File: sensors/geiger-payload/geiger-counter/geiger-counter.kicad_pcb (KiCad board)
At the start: 2 copper layers, 121.3 x 44.7 mm, 38 parts, among them J1 3531, J2 3531, J4 Conn_02x03_Odd_Even, J5 Conn_01x06, J6 Conn_01x03, Q1 MMBTA44, Q2 MMBT3904, Q3 MMBT3904, SW1 SW_Push, SW2 SW_SPDT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

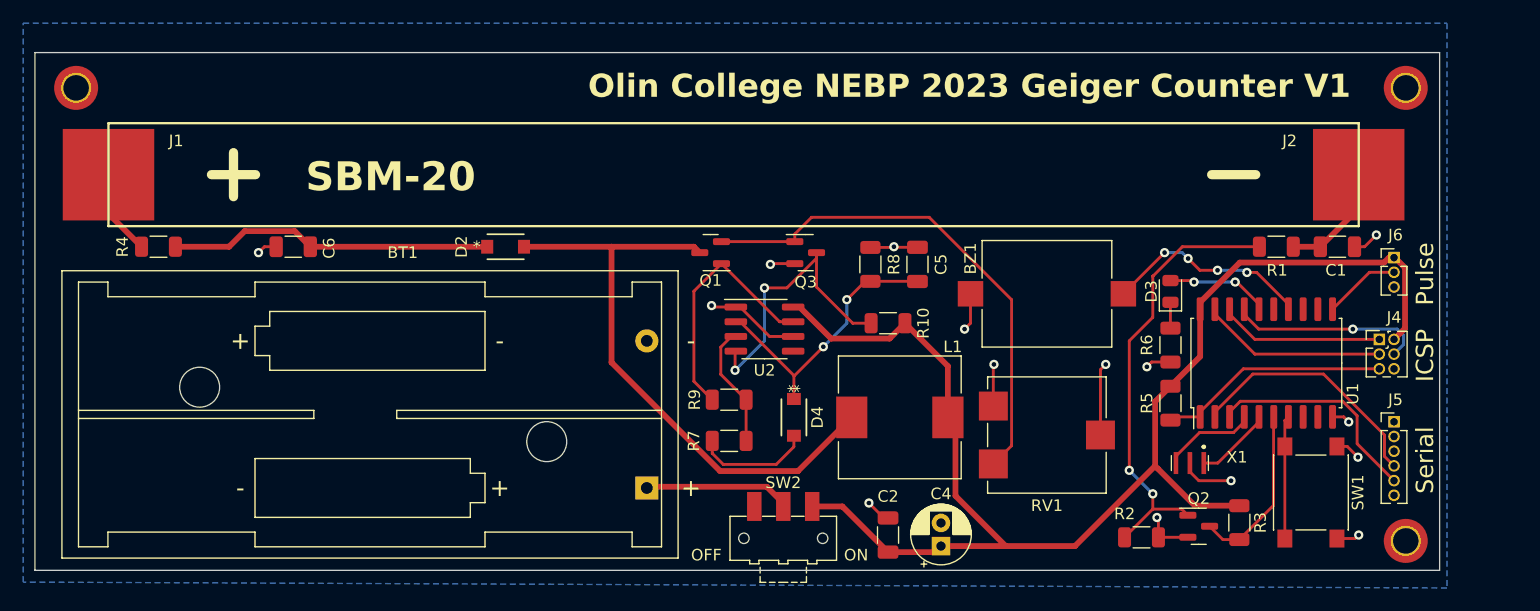
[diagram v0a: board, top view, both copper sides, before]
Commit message: Add pcb corrections
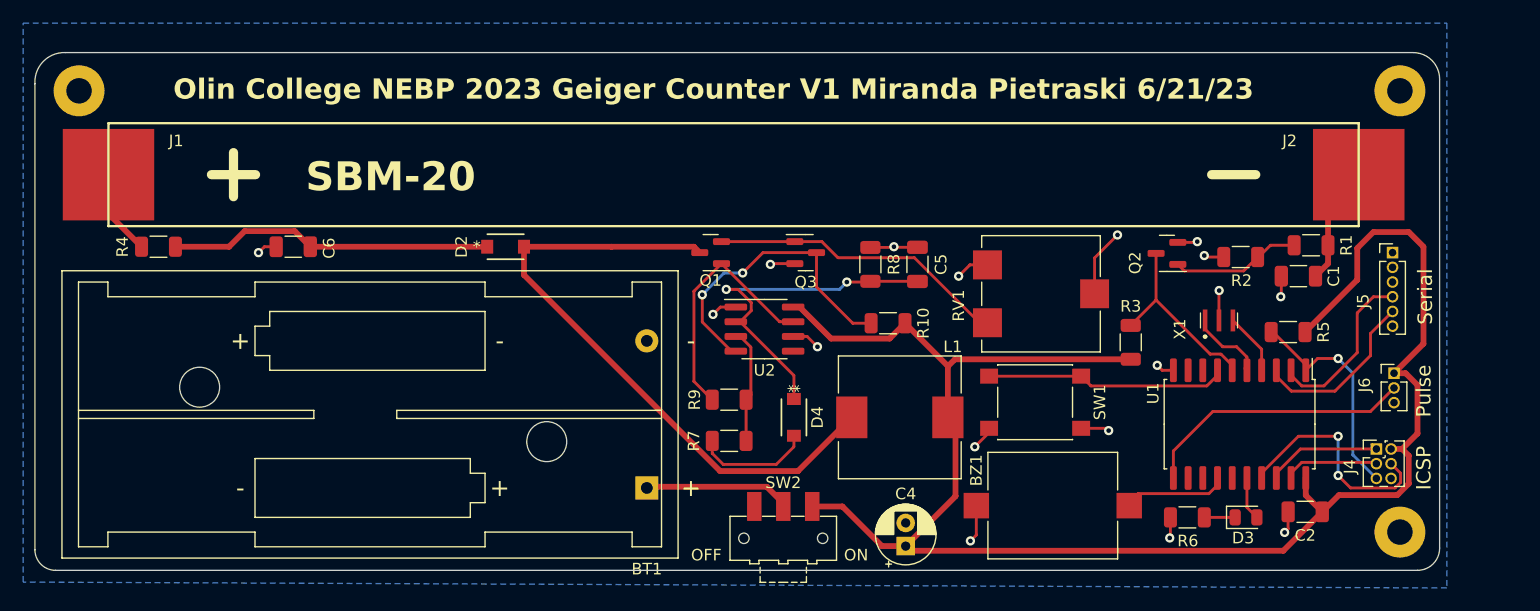
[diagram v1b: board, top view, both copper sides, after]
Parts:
- H1, H2, H3: value MountingHole -> MountingHole_Pad; footprint MountingHole:MountingHole_2.2mm_M2_DIN965_Pad_TopOnly -> MountingHole:MountingHole_2.2mm_M2_Pad
- moved C2 36.1 mm to (198.6, 64.0), turned to 180 degrees
- moved R2 25.7 mm to (193.0, 42.0), turned to 0 degrees
- moved SW1 25.1 mm to (175.3, 54.6), turned to 0 degrees
- moved Q2 23.7 mm to (186.6, 41.7), turned to 180 degrees
- moved D3 20.6 mm to (193.5, 64.5), turned to 0 degrees
- moved BZ1 18.3 mm to (176.8, 63.5)
- moved R3 18.2 mm to (183.5, 49.4), turned to 90 degrees
- moved R6 14.9 mm to (188.4, 64.5), turned to 180 degrees
- moved J5 14.6 mm to (206.1, 41.7)
- moved RV1 12.2 mm to (175.8, 45.2)
- moved R5 11.9 mm to (197.1, 48.5), turned to 180 degrees
- moved X1 11.7 mm to (191.1, 47.9), turned to 0 degrees
- moved J6 9.99 mm to (206.2, 52.1)
- moved J4 9.47 mm to (204.7, 58.6)
- moved U1 5.76 mm to (192.9, 56.5), turned to -90 degrees
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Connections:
- H1 pad 1: (no net) -> GND
- H2 pad 1: (no net) -> GND
- H3 pad 1: (no net) -> GND
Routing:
- net VCC: track 119.2 -> 149.8 mm
- net Net-(Q2-B): track 38.8 -> 11.2 mm, vias 2 -> 0
- net Net-(Q1-E): track 44.1 -> 25.9 mm
- net Net-(J6-Pin_2): track 6.63 -> 23.9 mm
- net Net-(U1-PD3): track 10.6 -> 21.4 mm
- net Net-(BZ1--): track 18.0 -> 9.12 mm, vias 4 -> 0
- net GND: track 50.7 -> 42.8 mm, vias 15 -> 17
- net Net-(J4-Pin_3): track 16.1 -> 8.22 mm
- net Net-(U2-TR): track 24.2 -> 30.9 mm
- net Net-(J5-Pin_4): track 21.6 -> 15.3 mm
- net Net-(D3-A): track 8.92 -> 3.76 mm, vias 2 -> 0
- net Net-(J5-Pin_5): track 19.3 -> 15.0 mm
- net Net-(J4-Pin_1): track 14.3 -> 10.5 mm
- net Net-(Q1-C): track 51.9 -> 55.1 mm
- net Net-(U1-PA1/XTAL2): track 8.15 -> 5.33 mm
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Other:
- outline, holes or cut-outs redrawn
- board text added: "Olin College NEBP 2023 Geiger Counter V1 Miranda Pietraski 6/21/23"
- board text removed: "Olin College NEBP 2023 Geiger Counter V1"

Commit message: add board fixes
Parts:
- moved H2 0.97 mm to (206.4, 26.8)
- moved H3 0.90 mm to (92.8, 26.8)
- moved H1 0.38 mm to (206.4, 65.8)
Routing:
- net Net-(Q1-E): track 25.9 -> 27.8 mm
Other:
- board size 121.3 x 44.7 mm -> 121.3 x 46.1 mm
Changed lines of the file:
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@@
   )
   (footprint "MountingHole:MountingHole_2.2mm_M2_Pad" (layer "F.Cu")
-    (at 206.756 65.786)
+    (at 206.375 65.786)
     (descr "Mounting Hole 2.2mm, M2")
     (tags "mounting hole 2.2mm m2")
@@
   )
   (footprint "MountingHole:MountingHole_2.2mm_M2_Pad" (layer "F.Cu")
-    (at 92.71 27.686)
+    (at 92.837 26.797)
     (descr "Mounting Hole 2.2mm, M2")
     (tags "mounting hole 2.2mm m2")
@@
   )
   (footprint "MountingHole:MountingHole_2.2mm_M2_Pad" (layer "F.Cu")
-    (at 206.756 27.686)
+    (at 206.375 26.797)
     (descr "Mounting Hole 2.2mm, M2")
     (tags "mounting hole 2.2mm m2")
@@
   (gr_line (start 106.045 33.02) (end 106.045 36.83)
     (stroke (width 0.8) (type default)) (layer "F.SilkS"))
+  (gr_arc (start 88.9 26.543) (mid 89.858175 24.034993) (end 92.329 22.984649)
+    (stroke (width 0.1) (type default)) (layer "Edge.Cuts"))
   (gr_arc (start 90.678 69.088) (mid 89.420764 68.567236) (end 88.9 67.31)
-    (stroke (width 0.1) (type default)) (layer "Edge.Cuts"))
-  (gr_arc (start 88.901216 27.07334) (mid 89.633813 25.133633) (end 91.567 24.384)
     (stroke (width 0.1) (type default)) (layer "Edge.Cuts"))
   (gr_arc (start 210.185 67.183) (mid 209.627038 68.530038) (end 208.28 69.088)
     (stroke (width 0.1) (type default)) (layer "Edge.Cuts"))
-  (gr_arc (start 207.899 24.384) (mid 209.515446 25.053554) (end 210.185 26.67)
+  (gr_line (start 92.329 22.984649) (end 207.391 22.987)
     (stroke (width 0.1) (type default)) (layer "Edge.Cuts"))
-  (gr_line (start 210.185 67.183) (end 210.185 26.67)
+  (gr_arc (start 207.391 22.987) (mid 209.366656 23.805344) (end 210.185 25.781)
     (stroke (width 0.1) (type default)) (layer "Edge.Cuts"))
-  (gr_line (start 88.901216 27.07334) (end 88.9 67.31)
+  (gr_line (start 210.185 67.183) (end 210.185 25.781)
     (stroke (width 0.1) (type default)) (layer "Edge.Cuts"))
-  (gr_line (start 207.899 24.384) (end 91.567 24.384)
+  (gr_line (start 88.9 26.543) (end 88.9 67.31)
     (stroke (width 0.1) (type default)) (layer "Edge.Cuts"))
   (gr_line (start 90.678 69.088) (end 208.28 69.088)
@@
     (effects (font (size 1.25 1.25) (thickness 0.1875)) (justify left bottom))
   )
-  (gr_text "Olin College NEBP 2023 Geiger Counter V1 Miranda Pietraski 6/21/23" (at 100.838 28.575) (layer "F.SilkS")
+  (gr_text "Olin College NEBP 2023 Geiger Counter V1 Miranda Pietraski 6/21/23" (at 100.965 27.94) (layer "F.SilkS")
     (effects (font (size 1.75 1.75) (thickness 0.35) bold) (justify left bottom))
   )
@@
   (segment (start 148.179 42.606) (end 153.198 47.625) (width 0.25) (layer "F.Cu") (net 21))
   (segment (start 148.179 42.606) (end 145.796 44.989) (width 0.25) (layer "F.Cu") (net 21))
-  (segment (start 158.235751 42.097) (end 156.844751 40.706) (width 0.25) (layer "F.Cu") (net 22))
+  (segment (start 170.648 47.712) (end 171.143 47.712) (width 0.25) (layer "F.Cu") (net 22))
+  (segment (start 166.027 40.297) (end 167.386 41.656) (width 0.25) (layer "F.Cu") (net 22))
   (segment (start 148.179 40.706) (end 154.5105 40.706) (width 0.25) (layer "F.Cu") (net 22))
-  (segment (start 171.143 47.712) (end 170.453173 47.712) (width 0.25) (layer "F.Cu") (net 22))
-  (segment (start 164.838173 42.097) (end 158.235751 42.097) (width 0.25) (layer "F.Cu") (net 22))
-  (segment (start 156.844751 40.706) (end 154.5105 40.706) (width 0.25) (layer "F.Cu") (net 22))
-  (segment (start 170.453173 47.712) (end 164.838173 42.097) (width 0.25) (layer "F.Cu") (net 22))
+  (segment (start 154.9195 40.297) (end 166.027 40.297) (width 0.25) (layer "F.Cu") (net 22))
+  (segment (start 154.5105 40.706) (end 154.9195 40.297) (width 0.25) (layer "F.Cu") (net 22))
+  (segment (start 167.386 41.656) (end 167.386 44.45) (width 0.25) (layer "F.Cu") (net 22))
+  (segment (start 167.386 44.45) (end 170.648 47.712) (width 0.25) (layer "F.Cu") (net 22))
   (segment (start 193.271 43.237) (end 194.471 42.037) (width 0.25) (layer "F.Cu") (net 23))
   (segment (start 194.471 42.037) (end 194.564 42.037) (width 0.25) (layer "F.Cu") (net 23))
